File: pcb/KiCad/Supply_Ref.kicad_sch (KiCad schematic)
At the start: 39 parts, among them J9 RF_Shield_One_Piece, U1 LT3045EMSE, U2 LT3094EMSE, U3 LT1236-10, U6 LT8610

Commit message: Cleanup
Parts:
- RV1: footprint custom:Pin_Header_Straight_1x03_Pitch2.54mm_Friction_Lock -> Connector_Molex:Molex_KK-254_AE-6410-03A_1x03_P2.54mm_Vertical
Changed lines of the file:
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@@
       (effects (font (size 1.27 1.27)) (justify right))
     )
-    (property "Footprint" "custom:Pin_Header_Straight_1x03_Pitch2.54mm_Friction_Lock" (at 232.41 43.18 0)
+    (property "Footprint" "Connector_Molex:Molex_KK-254_AE-6410-03A_1x03_P2.54mm_Vertical" (at 232.41 43.18 0)
       (effects (font (size 1.27 1.27)) hide)
     )

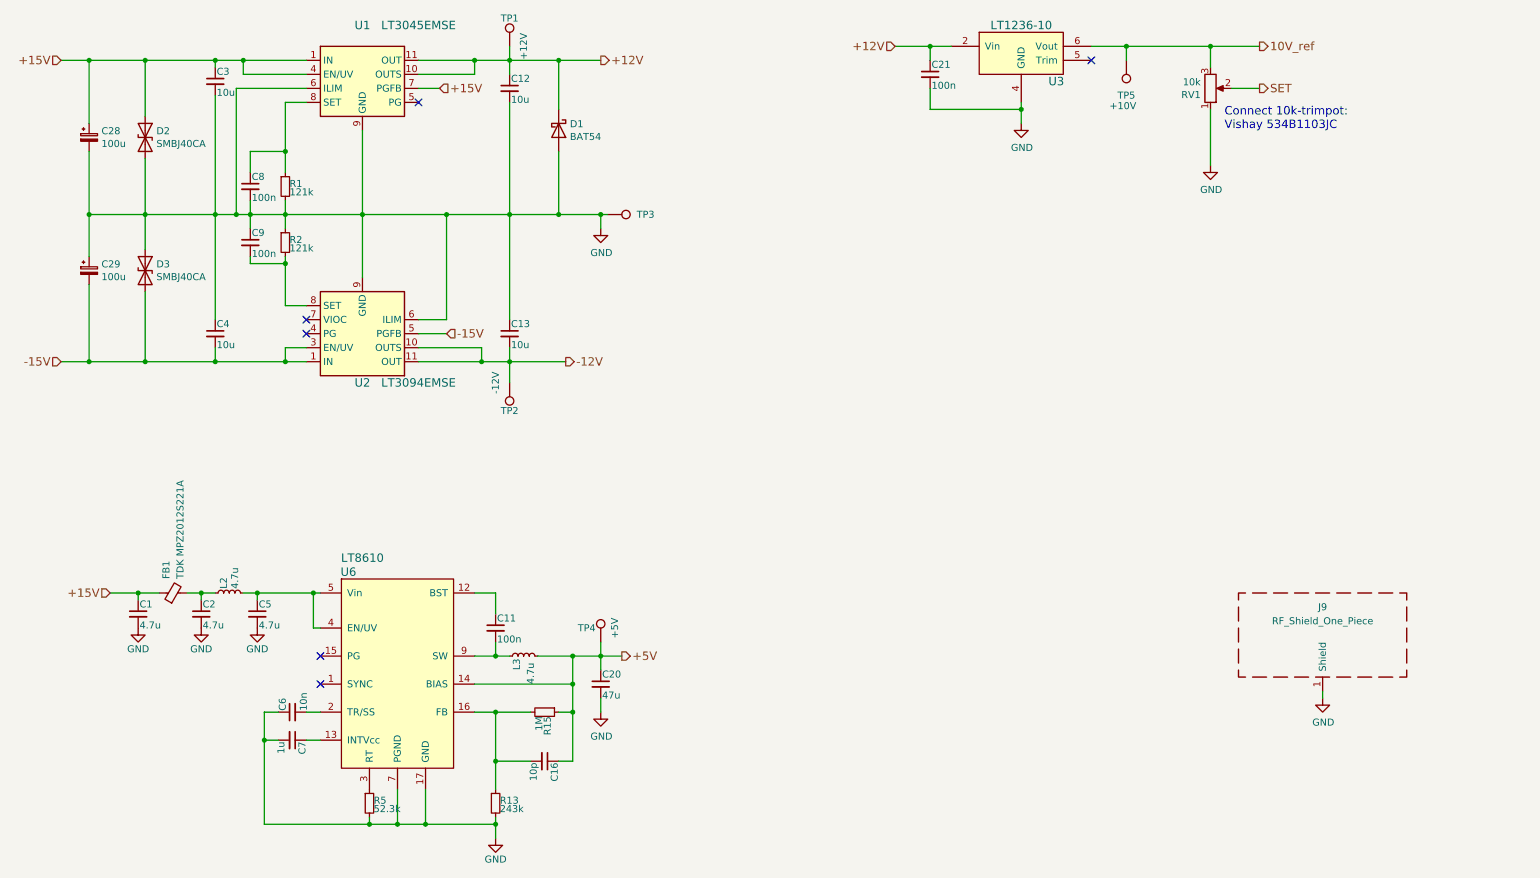
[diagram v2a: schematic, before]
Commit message: Updated to KiCad 8 (#8)
* Updated to KiCad 8
* Added assembly instructions for the potentiometer
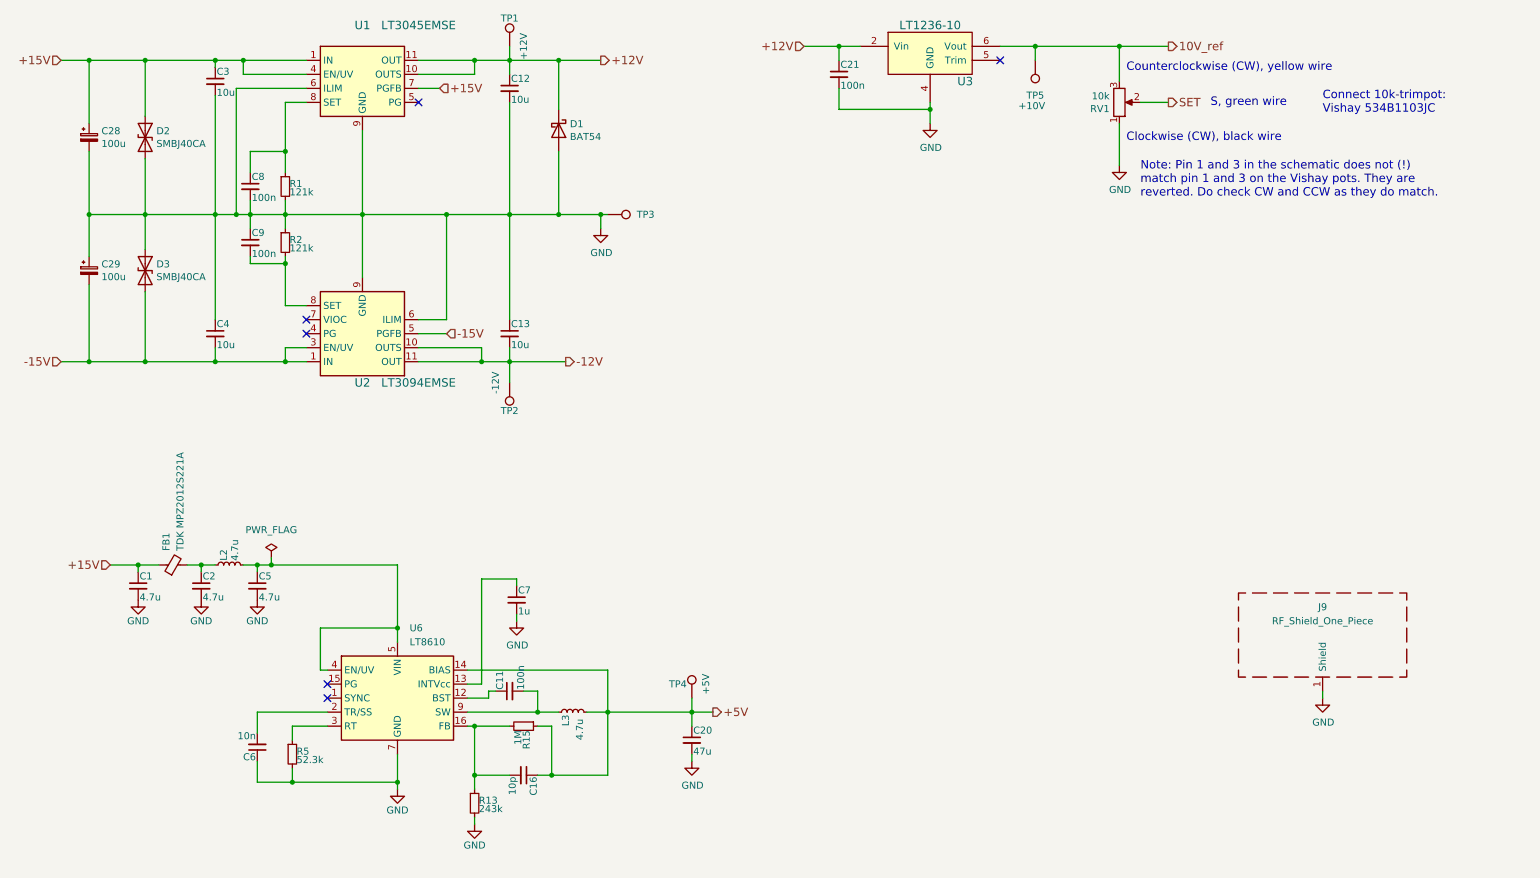
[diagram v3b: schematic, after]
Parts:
- removed U6: LT8610, Package_SO:MSOP-16-1EP_3x4.039mm_P0.5mm_EP1.651x2.845mm, symbol LinearTechnology:LT8610
- added U6: LT8610, Package_SO:MSOP-16-1EP_3x4.039mm_P0.5mm_EP1.651x2.845mm, symbol Regulator_Switching:LT8610
- L2, L3: footprint custom:Coilcraft_MSS1278T -> Inductor_SMD:L_Coilcraft_MSS1278T-XXX
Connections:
- net +5V: now also U6.14 (BIAS)
- net GND: now also U6.17 (GND), U6.7 (GND), U6.8 (GND)
- net at C11.2, L3.1: now also U6.10 (SW), U6.11 (SW), U6.9 (SW)
- net at C11.1: now also U6.12 (BST)
- net at C7.1: now also U6.13 (INTVcc)
- net at C16.2, R13.1, R15.2: now also U6.16 (FB)
- net at C6.2: now also U6.2 (TR/SS)
- net at R5.1: now also U6.3 (RT)
- net at C5.1, L2.2: now also U6.4 (EN/UV), U6.5 (VIN), U6.6 (VIN)
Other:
- note added: "Clockwise (CW), black wire"
- note added: "Counterclockwise (CW), yellow wire"
- note added: "Note: Pin 1 and 3 in the schematic does not (!) match pin 1 and 3 on the Vishay pots. They are reverted. Do check CW and CCW as they do match."
- note added: "S, green wire"
- moved on the sheet: C1, C2, C21, C5, FB1, L2, RV1, TP5, U3
